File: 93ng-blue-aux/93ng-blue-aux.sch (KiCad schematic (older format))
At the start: 4 parts, among them U1 ESP32-WROOM-32D, U2 MCP1703A-3302_SOT223, U3 MC33897

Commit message: Finished first draft of schematic. Made symbol for new LDO
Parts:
- removed U2: MCP1703A-3302_SOT223, Package_TO_SOT_SMD:SOT-223-3_TabPin2, symbol Regulator_Linear:MCP1703A-3302_SOT223
- added C? (x2): 0.1uF, symbol Device:C_Small
- added C?: 47pF, symbol Device:C_Small
- added C?: 4.7uF, symbol Device:C_Small
- added D?: MMBZ15VDLT1, Package_TO_SOT_SMD:SOT-23, symbol Diode:MMBZxx
- added D?: D, symbol Device:D
- added D? (x2): LED, symbol Device:LED
- added J?: 12V INPUT, symbol Connector:Conn_01x02_Male
- added J?: ESP32 UART, symbol Connector:Conn_01x03_Male
- added J?: ESP32 JTAG, symbol Connector:Conn_01x04_Male
- added J?: AUX OUT, symbol Connector:AudioJack3
- added J?: MIC IN, symbol Connector:AudioJack3
- added L?: 47uH, symbol Device:L_Small
- added R? (x4): 100, symbol Device:R_Small
- added R? (x3): 1k, symbol Device:R_Small
- added R?: 2.7k, symbol Device:R_Small
- added R?: 10k, symbol Device:R_Small
- added R?: 6.49k, symbol Device:R_Small
- added SW?: ESP32 BOOT OPTION, symbol Switch:SW_SPDT
- added TP?: BM62_TX, symbol Connector:TestPoint
- added TP?: BM62_RX, symbol Connector:TestPoint
- added TP?: TX_COND, symbol Connector:TestPoint
- added TP?: FWD, symbol Connector:TestPoint
- added TP?: PLAY/PAUSE, symbol Connector:TestPoint
- added TP?: REV, symbol Connector:TestPoint
- added TP?: VOL-, symbol Connector:TestPoint
- added TP?: VOL+, symbol Connector:TestPoint
- added U?: BA33DD0T, symbol custom_symbols:BA33DD0T
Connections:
- net labels added: 3.3V, BM62_BT_WAKE, BM62_MCU_WAKE, BM62_RX, BM62_TX, GND, MC33_MODE0, MC33_MODE1, MC33_RX, MC33_TX, SW_CAN
- wire segments 0 -> 98
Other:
- note added: "12V TO 3.3V\n2A OUTPUT"
- note added: "BLUETOOTH AUDIO MODULE"
- note added: "MCU\nESP32 BASED\nARDUINO-COMPATIBLE"
- note added: "NOTE: USING ESP32 \nCAN CONTROLLER (SJA1000)"
- note added: "POWER SUPPLY"
- note added: "Single Wire CAN Transceiver\n33.33 kbps"
- moved on the sheet: U3, U?

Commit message: More work on schematic, focus on debugging utility, and started layout of PCB. Made footprint for BM62.
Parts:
- removed SW?: ESP32 BOOT OPTION, symbol Switch:SW_SPDT
- removed TP?: BM62_TX, symbol Connector:TestPoint
- removed TP?: BM62_RX, symbol Connector:TestPoint
- added J6: BM62 UART, Connector_PinHeader_2.54mm:PinHeader_1x03_P2.54mm_Vertical, symbol Connector:Conn_01x03_Male
- added SW1: SYS CONFIG, Button_Switch_SMD:SW_DIP_SPSTx04_Slide_Omron_A6S-410x_W8.9mm_P2.54mm, symbol Switch:SW_DIP_x04
- C1, C2, C3, C4: renamed from C?; footprint (none) -> Capacitor_SMD:C_0805_2012Metric_Pad1.15x1.40mm_HandSolder
- D1: renamed from D?; footprint (none) -> Diode_SMD:D_0805_2012Metric_Pad1.15x1.40mm_HandSolder
- D2, D4: renamed from D?; footprint (none) -> LED_SMD:LED_0805_2012Metric_Pad1.15x1.40mm_HandSolder
- J1: renamed from J?; footprint (none) -> Connector_PinHeader_2.54mm:PinHeader_1x02_P2.54mm_Vertical
- J2: renamed from J?; footprint (none) -> Connector_PinHeader_2.54mm:PinHeader_1x03_P2.54mm_Vertical
- J3: renamed from J?; footprint (none) -> Connector_PinHeader_2.54mm:PinHeader_1x04_P2.54mm_Vertical
- J4, J5: renamed from J?; footprint (none) -> Connector_Audio:Jack_3.5mm_CUI_SJ-3523-SMT_Horizontal
- L1: renamed from L?; footprint (none) -> Inductor_SMD:L_0805_2012Metric_Pad1.15x1.40mm_HandSolder
- R1, R10, R2, R3, R4, R5, R6, R7, R8, R9: renamed from R?; footprint (none) -> Resistor_SMD:R_0805_2012Metric_Pad1.15x1.40mm_HandSolder
- TP1, TP2, TP3, TP4, TP5, TP6: renamed from TP?; footprint (none) -> TestPoint:TestPoint_Pad_D2.0mm
- U2: renamed from U?; footprint (none) -> Package_TO_SOT_THT:TO-220-3_Vertical
- U3: footprint custom_footprints:MC33897 -> Package_SO:SOIC-14_3.9x8.7mm_P1.27mm
- U4: renamed from U?; footprint (none) -> custom_footprints:BM62SPKS1MC2-0001AA
- gave numbers to parts that had none: 1
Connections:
- net labels added: BM62_EAN, BM62_P2_0, BM62_P2_4, ESP32_BOOTOPT
- wire segments 98 -> 101
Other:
- note added: "SYSTEM CONFIG SWITCHES\nUSED TO PUT ESP32 OR BM62\nINTO PROGRAM MODE"
- moved on the sheet: C1, U2

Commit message: Added picture of schematic. Added some screw terminals.
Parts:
- removed J1: 12V INPUT, Connector_PinHeader_2.54mm:PinHeader_1x02_P2.54mm_Vertical, symbol Connector:Conn_01x02_Male
- added J1: 12V INPUT, TerminalBlock_Phoenix:TerminalBlock_Phoenix_MKDS-3-2-5.08_1x02_P5.08mm_Horizontal, symbol Connector:Screw_Terminal_01x02
- added J7: I-BUS, TerminalBlock_Phoenix:TerminalBlock_Phoenix_MKDS-3-2-5.08_1x02_P5.08mm_Horizontal, symbol Connector:Screw_Terminal_01x02
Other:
- moved on the sheet: C1, C2, C3, C4, D1, D2, D3, D4, J4, J5, J6, L1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

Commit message: Completed roughest PCB layout ever
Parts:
- U1: symbol RF_Module:ESP32-WROOM-32D -> 93ng-blue-aux-rescue:ESP32-WROOM-32D-RF_Module
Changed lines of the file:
@@
 EESchema Schematic File Version 4
+LIBS:93ng-blue-aux-cache
 EELAYER 30 0
 EELAYER END
@@
 $EndDescr
 $Comp
-L RF_Module:ESP32-WROOM-32D U1
+L 93ng-blue-aux-rescue:ESP32-WROOM-32D-RF_Module U1
 U 1 1 5E395DE5
 P 2500 4550

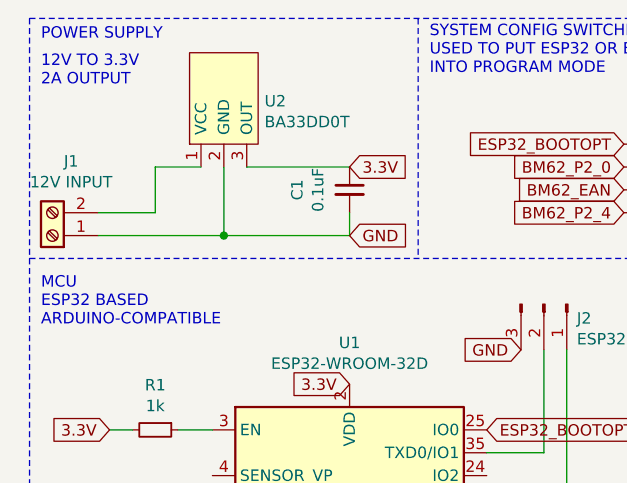
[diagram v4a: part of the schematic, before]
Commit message: Added 12V input filter cap
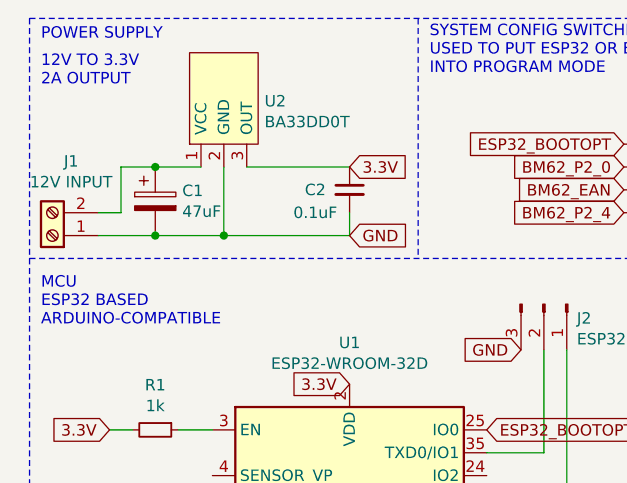
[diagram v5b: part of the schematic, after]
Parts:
- added C1: 47uF, symbol Device:CP
- renumbered C1 to C2
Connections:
- net GND: now also C1.2
- net at J1.2 (Pin_2), U2.1 (VCC): now also C1.1
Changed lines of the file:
@@
 	1    0    0    -1
 $EndComp
-Wire Wire Line
-	1400 2400 1650 2400
-Wire Wire Line
-	1650 2400 1650 2200
-$Comp
-L Device:C_Small C1
+$Comp
+L Device:C_Small C2
 U 1 1 5E3AE258
 P 2500 2300
-F 0 "C1" V 2271 2300 50  0000 C CNN
-F 1 "0.1uF" V 2362 2300 50  0000 C CNN
+F 0 "C2" H 2350 2300 50  0000 C CNN
+F 1 "0.1uF" H 2350 2200 50  0000 C CNN
 F 2 "Capacitor_SMD:C_0805_2012Metric_Pad1.15x1.40mm_HandSolder" H 2500 2300 50  0001 C CNN
 F 3 "~" H 2500 2300 50  0001 C CNN
@@
 	1950 2200 1950 2500
 Wire Wire Line
-	1400 2500 1950 2500
+	1400 2500 1650 2500
 Wire Wire Line
 	1950 2500 2500 2500
@@
 Wire Notes Line
 	1100 1550 4650 1550
+$Comp
+L Device:CP C1
+U 1 1 5E4E29F0
+P 1650 2350
+F 0 "C1" H 1768 2396 50  0000 L CNN
+F 1 "47uF" H 1768 2305 50  0000 L CNN
+F 2 "" H 1688 2200 50  0001 C CNN
+F 3 "~" H 1650 2350 50  0001 C CNN
+	1    1650 2350
+	1    0    0    -1
+$EndComp
+Connection ~ 1650 2500
+Wire Wire Line
+	1650 2500 1950 2500
+Wire Wire Line
+	1650 2200 1500 2200
+Wire Wire Line
+	1500 2200 1500 2400
+Wire Wire Line
+	1500 2400 1400 2400
+Connection ~ 1650 2200
 $EndSCHEMATC

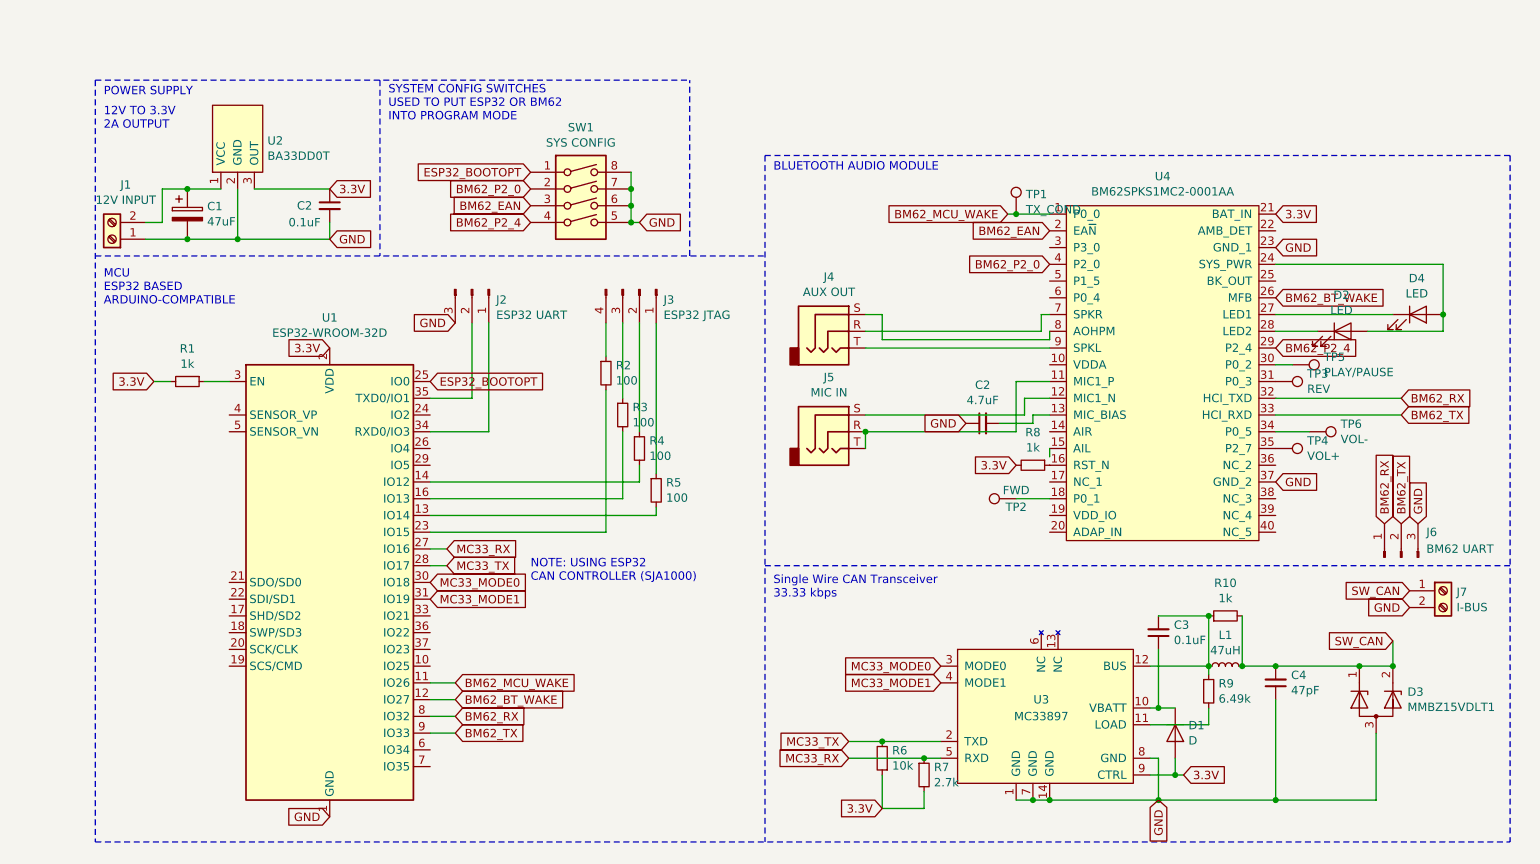
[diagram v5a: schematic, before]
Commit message: Working on 100mmx100mm board design. Adjusted input power filter cap size. Re-designed bluetooth antenna keepout comment, and added courtyard to module.
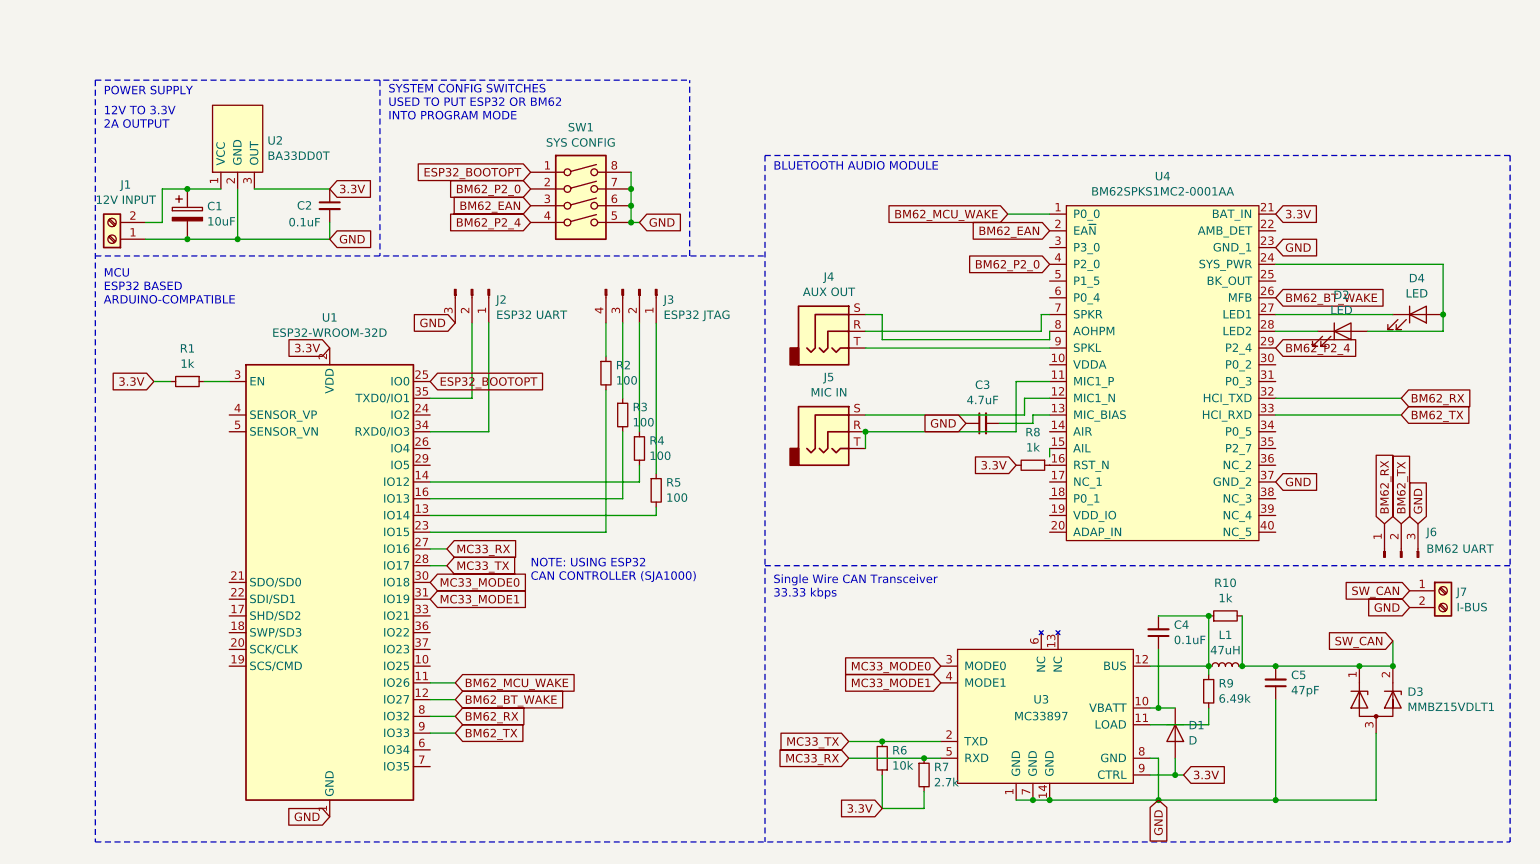
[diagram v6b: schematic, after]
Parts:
- removed TP1: TX_COND, TestPoint:TestPoint_Pad_D2.0mm, symbol Connector:TestPoint
- removed TP2: FWD, TestPoint:TestPoint_Pad_D2.0mm, symbol Connector:TestPoint
- removed TP3: REV, TestPoint:TestPoint_Pad_D2.0mm, symbol Connector:TestPoint
- removed TP4: VOL+, TestPoint:TestPoint_Pad_D2.0mm, symbol Connector:TestPoint
- removed TP5: PLAY/PAUSE, TestPoint:TestPoint_Pad_D2.0mm, symbol Connector:TestPoint
- removed TP6: VOL-, TestPoint:TestPoint_Pad_D2.0mm, symbol Connector:TestPoint
- C1: value 47uF -> 10uF; footprint (none) -> Capacitor_THT:CP_Radial_D10.0mm_P5.00mm
- renumbered C2 to C3, C3 to C4, C4 to C5
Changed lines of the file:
@@
 	7950 4750 7950 5050
 $Comp
-L Device:C_Small C3
+L Device:C_Small C4
 U 1 1 5E410D36
 P 7450 4850
-F 0 "C3" H 7358 4804 50  0000 R CNN
+F 0 "C4" H 7358 4804 50  0000 R CNN
 F 1 "0.1uF" H 7358 4895 50  0000 R CNN
 F 2 "Capacitor_SMD:C_0805_2012Metric_Pad1.15x1.40mm_HandSolder" H 7450 4850 50  0001 C CNN
@@
 Connection ~ 6800 5850
 $Comp
-L Device:C_Small C4
+L Device:C_Small C5
 U 1 1 5E42115E
 P 8150 5150
-F 0 "C4" H 8058 5104 50  0000 R CNN
+F 0 "C5" H 8058 5104 50  0000 R CNN
 F 1 "47pF" H 8058 5195 50  0000 R CNN
 F 2 "Capacitor_SMD:C_0805_2012Metric_Pad1.15x1.40mm_HandSolder" H 8150 5150 50  0001 C CNN
@@
 Connection ~ 5700 3650
 $Comp
-L Device:C_Small C2
+L Device:C_Small C3
 U 1 1 5E45FD4C
 P 6400 3600
-F 0 "C2" V 6629 3600 50  0000 C CNN
+F 0 "C3" V 6629 3600 50  0000 C CNN
 F 1 "4.7uF" V 6538 3600 50  0000 C CNN
 F 2 "Capacitor_SMD:C_0805_2012Metric_Pad1.15x1.40mm_HandSolder" H 6400 3600 50  0001 C CNN
@@
 Wire Wire Line
 	8150 3550 8900 3550
-$Comp
-L Connector:TestPoint TP1
-U 1 1 5E47DF3A
-P 6600 2350
-F 0 "TP1" H 6658 2468 50  0000 L CNN
-F 1 "TX_COND" H 6658 2377 50  0000 L CNN
-F 2 "TestPoint:TestPoint_Pad_D2.0mm" H 6800 2350 50  0001 C CNN
-F 3 "~" H 6800 2350 50  0001 C CNN
-	1    6600 2350
-	1    0    0    -1
-$EndComp
-Wire Wire Line
-	6800 2350 6600 2350
-Connection ~ 6600 2350
-Wire Wire Line
-	6600 2350 6550 2350
-$Comp
-L Connector:TestPoint TP2
-U 1 1 5E480A36
-P 6600 4050
-F 0 "TP2" V 6550 4050 50  0000 C CNN
-F 1 "FWD" V 6650 4050 50  0000 C CNN
-F 2 "TestPoint:TestPoint_Pad_D2.0mm" H 6800 4050 50  0001 C CNN
-F 3 "~" H 6800 4050 50  0001 C CNN
-	1    6600 4050
-	0    -1   -1   0
-$EndComp
-Wire Wire Line
-	6600 4050 6800 4050
-$Comp
-L Connector:TestPoint TP5
-U 1 1 5E483497
-P 8250 3250
-F 0 "TP5" V 8204 3438 50  0000 L CNN
-F 1 "PLAY/PAUSE" V 8295 3438 50  0000 L CNN
-F 2 "TestPoint:TestPoint_Pad_D2.0mm" H 8450 3250 50  0001 C CNN
-F 3 "~" H 8450 3250 50  0001 C CNN
-	1    8250 3250
-	0    1    1    0
-$EndComp
-Wire Wire Line
-	8150 3250 8250 3250
-$Comp
-L Connector:TestPoint TP3
-U 1 1 5E4863CC
-P 8150 3350
-F 0 "TP3" V 8104 3538 50  0000 L CNN
-F 1 "REV" V 8195 3538 50  0000 L CNN
-F 2 "TestPoint:TestPoint_Pad_D2.0mm" H 8350 3350 50  0001 C CNN
-F 3 "~" H 8350 3350 50  0001 C CNN
-	1    8150 3350
-	0    1    1    0
-$EndComp
-$Comp
-L Connector:TestPoint TP6
-U 1 1 5E486CEC
-P 8350 3650
-F 0 "TP6" V 8304 3838 50  0000 L CNN
-F 1 "VOL-" V 8395 3838 50  0000 L CNN
-F 2 "TestPoint:TestPoint_Pad_D2.0mm" H 8550 3650 50  0001 C CNN
-F 3 "~" H 8550 3650 50  0001 C CNN
-	1    8350 3650
-	0    1    1    0
-$EndComp
-Wire Wire Line
-	8150 3650 8350 3650
-$Comp
-L Connector:TestPoint TP4
-U 1 1 5E48E99A
-P 8150 3750
-F 0 "TP4" V 8104 3938 50  0000 L CNN
-F 1 "VOL+" V 8195 3938 50  0000 L CNN
-F 2 "TestPoint:TestPoint_Pad_D2.0mm" H 8350 3750 50  0001 C CNN
-F 3 "~" H 8350 3750 50  0001 C CNN
-	1    8150 3750
-	0    1    1    0
-$EndComp
 Wire Wire Line
 	6800 3750 6800 3800
@@
 P 1650 2350
 F 0 "C1" H 1768 2396 50  0000 L CNN
-F 1 "47uF" H 1768 2305 50  0000 L CNN
-F 2 "" H 1688 2200 50  0001 C CNN
+F 1 "10uF" H 1768 2305 50  0000 L CNN
+F 2 "Capacitor_THT:CP_Radial_D10.0mm_P5.00mm" H 1688 2200 50  0001 C CNN
 F 3 "~" H 1650 2350 50  0001 C CNN
 	1    1650 2350
@@
 	1500 2400 1400 2400
 Connection ~ 1650 2200
+Wire Wire Line
+	6550 2350 6800 2350
 $EndSCHEMATC
